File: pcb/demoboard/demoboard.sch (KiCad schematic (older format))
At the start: 32 parts, among them J1 BTN, J10 Conn_01x15, J11 Servo2, J12 TEMP, J13 MOT_A, J14 MOT_B, J15 CAP_T, J16 ANALOG, J17 7SEG1, J18 7SEG2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

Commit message: PCB 0.1
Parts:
- removed J15: CAP_T, Connector_PinSocket_2.54mm:PinSocket_1x04_P2.54mm_Vertical, symbol Connector_Generic:Conn_01x04
- removed J21: BITS, Connector_PinSocket_2.54mm:PinSocket_1x10_P2.54mm_Vertical, symbol Connector_Generic:Conn_01x10
- removed U3: PCF8574, Package_DIP:DIP-16_W7.62mm, symbol Interface_Expansion:PCF8574
- added R5: 4K7, Resistor_THT:R_Axial_DIN0207_L6.3mm_D2.5mm_P10.16mm_Horizontal, symbol Device:R
- added U1: 74HC595, Package_DIP:DIP-16_W7.62mm, symbol 74xx:74HC595
- J1: footprint Connector_PinSocket_2.54mm:PinSocket_1x03_P2.54mm_Vertical -> Connector_PinSocket_2.54mm:PinSocket_1x03_P2.54mm_Horizontal
- R2, R3: value 4K7 -> 220R; footprint Resistor_THT:R_Axial_DIN0207_L6.3mm_D2.5mm_P10.16mm_Horizontal -> Resistor_THT:R_Axial_DIN0207_L6.3mm_D2.5mm_P2.54mm_Vertical
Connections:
- net D35 is gone; now on net BTN: J10.11 (Pin_11), J8.11 (Pin_11)
- net INT is gone; now on net BTN: J4.3 (Pin_3)
- net B0: now also J18.1 (Pin_1), U1.15 (QA); no longer J17.1 (Pin_1)
- net B1: now also J18.2 (Pin_2), U1.1 (QB); no longer J17.2 (Pin_2)
- net B2: now also J17.1 (Pin_1), U1.2 (QC); no longer J17.3 (Pin_3)
- net B3: now also U1.3 (QD)
- net B4: now also J17.3 (Pin_3), U1.4 (QE); no longer J17.5 (Pin_5)
- net B5: now also J18.5 (Pin_5), U1.5 (QF); no longer J18.1 (Pin_1)
- net B6: now also J17.2 (Pin_2), U1.6 (QG); no longer J18.2 (Pin_2)
- net B7: now also J17.5 (Pin_5), U1.7 (QH); no longer J18.5 (Pin_5)
- net BTN: no longer J3.10 (Pin_10), J5.10 (Pin_10)
- net D14: now also R2.1; no longer J18.3 (Pin_3)
- net D2: now also J4.1 (Pin_1)
- net D21: no longer R3.1
- net D22: no longer R2.1
- net D25: now also R3.1; no longer J18.4 (Pin_4)
- net D32: now also J6.2 (Pin_2)
- net D33: now also U1.12 (RCLK)
- net D34: now also J4.2 (Pin_2)
- net D5: now also U2.15 (4A); no longer J6.2 (Pin_2)
- net GND: now also U1.13 (~OE), U1.8 (GND)
- net MA1Y: now also J13.2 (Pin_2); no longer J13.1 (Pin_1)
- net MA2Y: now also J13.1 (Pin_1); no longer J13.2 (Pin_2)
- net MB1Y: now also J14.2 (Pin_2); no longer J14.1 (Pin_1)
- net MB2Y: now also J14.1 (Pin_1); no longer J14.2 (Pin_2)
- net VCC: now also R5.2, U1.16 (VCC); no longer R2.2, R3.2
- net BUZZ renamed D23
- net D23: now also U1.14 (SER); no longer J4.1 (Pin_1)
- net D18 renamed CLK
- net CLK: now also U1.11 (SRCLK); no longer U2.15 (4A)
- new net: J18.3 (Pin_3), R3.2
- new net: J18.4 (Pin_4), R2.2
- new net D19: J3.10 (Pin_10), J5.10 (Pin_10)
- new net SRCLR: R5.1, U1.10 (~SRCLR)
- no-connect marks 1 -> 2

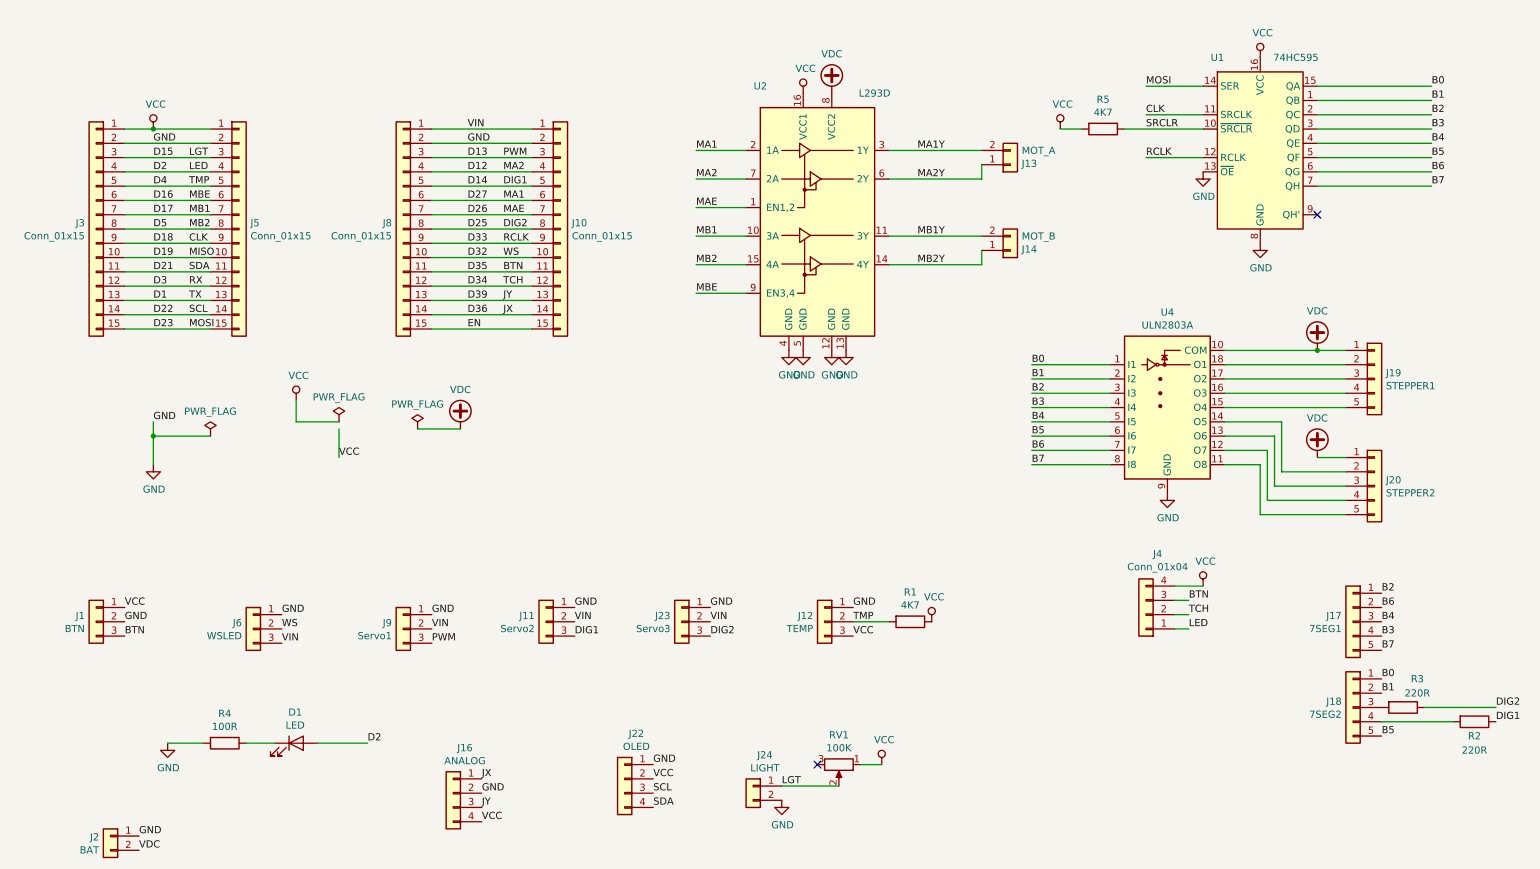
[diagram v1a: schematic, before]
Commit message: Rearrange the PCB components a bit
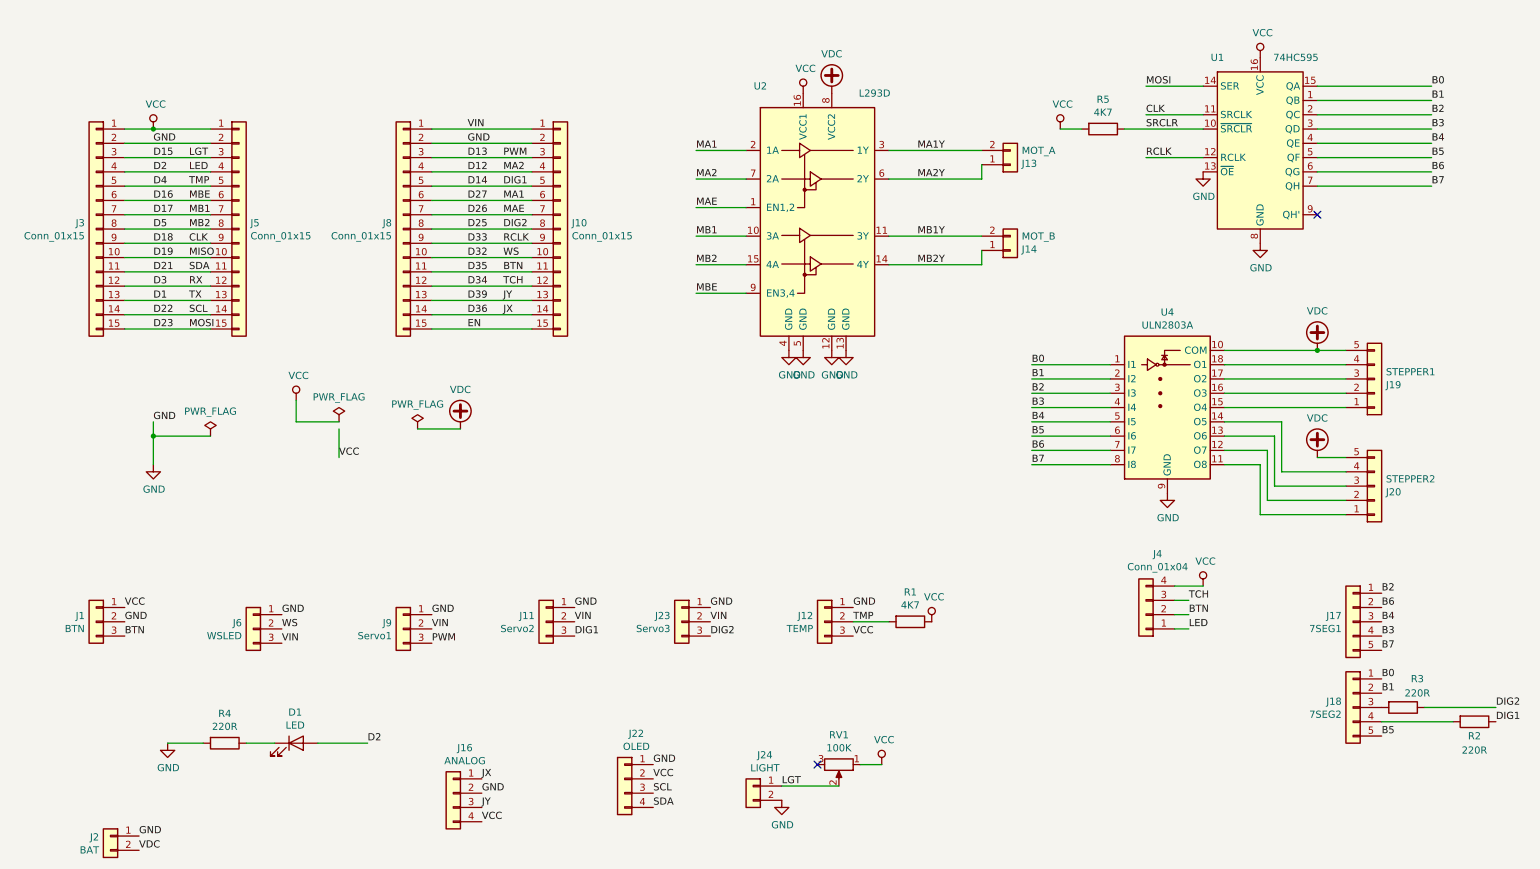
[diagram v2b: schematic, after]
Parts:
- R4: value 100R -> 220R
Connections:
- net BTN: now also J4.2 (Pin_2); no longer J4.3 (Pin_3)
- net D34: now also J4.3 (Pin_3); no longer J4.2 (Pin_2)
- net VDC: now also J19.5 (Pin_5), J20.5 (Pin_5); no longer J19.1 (Pin_1), J20.1 (Pin_1)
- net at U4.11 (O8): now also J20.1 (Pin_1); no longer J20.5 (Pin_5)
- net at U4.12 (O7): now also J20.2 (Pin_2); no longer J20.4 (Pin_4)
- net at U4.14 (O5): now also J20.4 (Pin_4); no longer J20.2 (Pin_2)
- net at U4.15 (O4): now also J19.1 (Pin_1); no longer J19.5 (Pin_5)
- net at U4.16 (O3): now also J19.2 (Pin_2); no longer J19.4 (Pin_4)
- net at U4.18 (O1): now also J19.4 (Pin_4); no longer J19.2 (Pin_2)
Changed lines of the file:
@@
 F 3 "~" H 10000 3800 50  0001 C CNN
 	1    10000 3800
-	1    0    0    -1
+	1    0    0    1
 $EndComp
 $Comp
@@
 F 3 "~" H 10000 4550 50  0001 C CNN
 	1    10000 4550
-	1    0    0    -1
+	1    0    0    1
 $EndComp
 $Comp
@@
 P 1950 6350
 F 0 "R4" V 1743 6350 50  0000 C CNN
-F 1 "100R" V 1834 6350 50  0000 C CNN
+F 1 "220R" V 1834 6350 50  0000 C CNN
 F 2 "Resistor_THT:R_Axial_DIN0207_L6.3mm_D2.5mm_P10.16mm_Horizontal" V 1880 6350 50  0001 C CNN
 F 3 "~" H 1950 6350 50  0001 C CNN
@@
 Wire Wire Line
 	8600 5350 8700 5350
-Text Label 8700 5350 0    50   ~ 0
+Text Label 8700 5450 0    50   ~ 0
 BTN
 $Comp
@@
 Text Label 8400 2050 0    50   ~ 0
 SRCLR
-Text Label 8700 5450 0    50   ~ 0
+Text Label 8700 5350 0    50   ~ 0
 TCH
 Text Label 6800 2400 0    50   ~ 0

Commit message: PCB v0.2
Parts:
- added J7: JMP, Connector_PinHeader_2.54mm:PinHeader_1x02_P2.54mm_Vertical, symbol Connector_Generic:Conn_01x02
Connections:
- net B6: now also J17.5 (Pin_5); no longer J17.2 (Pin_2)
- net B7: now also J17.2 (Pin_2); no longer J17.5 (Pin_5)
- net BTN: now also J4.3 (Pin_3); no longer J4.2 (Pin_2)
- net D13: now also J11.3 (Pin_3), R2.1; no longer J9.3 (Pin_3)
- net D14: now also J9.3 (Pin_3); no longer J11.3 (Pin_3), R2.1
- net D15: now also U2.9 (EN3,4); no longer J24.1 (Pin_1), RV1.2
- net D16: now also U2.10 (3A); no longer U2.9 (EN3,4)
- net D17: now also U2.15 (4A); no longer U2.10 (3A)
- net D25: now also J6.2 (Pin_2); no longer J23.3 (Pin_3), R3.1
- net D32: now also U1.12 (RCLK); no longer J6.2 (Pin_2)
- net D33: now also J4.2 (Pin_2); no longer U1.12 (RCLK)
- net D34: now also J24.1 (Pin_1), RV1.2; no longer J4.3 (Pin_3)
- net D5: now also J23.3 (Pin_3), R3.1; no longer U2.15 (4A)
- net GND: now also J7.1 (Pin_1)
- net VDC: now also J19.1 (Pin_1), J20.1 (Pin_1); no longer J19.5 (Pin_5), J20.5 (Pin_5)
- net at U4.11 (O8): now also J20.2 (Pin_2); no longer J20.1 (Pin_1)
- net at U4.12 (O7): now also J20.3 (Pin_3); no longer J20.2 (Pin_2)
- net at U4.13 (O6): now also J20.4 (Pin_4); no longer J20.3 (Pin_3)
- net at U4.14 (O5): now also J20.5 (Pin_5); no longer J20.4 (Pin_4)
- net at U4.15 (O4): now also J19.2 (Pin_2); no longer J19.1 (Pin_1)
- net at U4.16 (O3): now also J19.3 (Pin_3); no longer J19.2 (Pin_2)
- net at U4.17 (O2): now also J19.4 (Pin_4); no longer J19.3 (Pin_3)
- net at U4.18 (O1): now also J19.5 (Pin_5); no longer J19.4 (Pin_4)
- net at J18.3 (Pin_3): now also R2.2; no longer R3.2
- net at J18.4 (Pin_4): now also R3.2; no longer R2.2
- net RP: now reaches RV1.3
- net RP: now also J7.2 (Pin_2)
- no-connect marks 2 -> 1
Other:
- moved on the sheet: J19, J20, R2, R3
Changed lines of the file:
@@
 F 3 "~" H 6150 5500 50  0001 C CNN
 	1    6150 5500
-	-1   0    0    -1
+	-1   0    0    1
 $EndComp
 $Comp
 L Connector_Generic:Conn_01x05 J19
 U 1 1 5E2CC9BE
-P 10000 3800
-F 0 "J19" H 10080 3842 50  0000 L CNN
-F 1 "STEPPER1" H 10080 3751 50  0000 L CNN
-F 2 "Connector_PinHeader_2.54mm:PinHeader_1x05_P2.54mm_Vertical" H 10000 3800 50  0001 C CNN
-F 3 "~" H 10000 3800 50  0001 C CNN
-	1    10000 3800
+P 10000 3900
+F 0 "J19" H 10080 3942 50  0000 L CNN
+F 1 "STEPPER1" H 10080 3851 50  0000 L CNN
+F 2 "Connector_PinHeader_2.54mm:PinHeader_1x05_P2.54mm_Vertical" H 10000 3900 50  0001 C CNN
+F 3 "~" H 10000 3900 50  0001 C CNN
+	1    10000 3900
 	1    0    0    1
 $EndComp
@@
 L Connector_Generic:Conn_01x05 J20
 U 1 1 5E2CD0D9
-P 10000 4550
-F 0 "J20" H 10080 4592 50  0000 L CNN
-F 1 "STEPPER2" H 10080 4501 50  0000 L CNN
-F 2 "Connector_PinHeader_2.54mm:PinHeader_1x05_P2.54mm_Vertical" H 10000 4550 50  0001 C CNN
-F 3 "~" H 10000 4550 50  0001 C CNN
-	1    10000 4550
+P 10000 4650
+F 0 "J20" H 10080 4692 50  0000 L CNN
+F 1 "STEPPER2" H 10080 4601 50  0000 L CNN
+F 2 "Connector_PinHeader_2.54mm:PinHeader_1x05_P2.54mm_Vertical" H 10000 4650 50  0001 C CNN
+F 3 "~" H 10000 4650 50  0001 C CNN
+	1    10000 4650
 	1    0    0    1
 $EndComp
@@
 Text Label 5350 5600 0    50   ~ 0
 DIG2
-Text Label 6350 5400 0    50   ~ 0
+Text Label 6350 5600 0    50   ~ 0
 GND
 Text Label 6350 5500 0    50   ~ 0
 TMP
-Text Label 6350 5600 0    50   ~ 0
+Text Label 6350 5400 0    50   ~ 0
 VCC
 $Comp
@@
 Text Label 10050 5300 0    50   ~ 0
 B2
-Text Label 10050 5400 0    50   ~ 0
+Text Label 10050 5700 0    50   ~ 0
 B6
 Text Label 10050 5500 0    50   ~ 0
@@
 Text Label 10050 5600 0    50   ~ 0
 B3
-Text Label 10050 5700 0    50   ~ 0
+Text Label 10050 5400 0    50   ~ 0
 B7
 Text Label 10050 5900 0    50   ~ 0
@@
 Text Label 10050 6000 0    50   ~ 0
 B1
+Text Label 10850 6200 0    50   ~ 0
+DIG2
 Text Label 10850 6100 0    50   ~ 0
-DIG2
-Text Label 10850 6200 0    50   ~ 0
 DIG1
 Text Label 10050 6300 0    50   ~ 0
@@
 Wire Wire Line
 	3600 4150 3300 4150
-NoConn ~ 6100 6500
 $Comp
 L power:PWR_FLAG #FLG0103
@@
 Wire Wire Line
 	2450 4100 2750 4100
-Wire Wire Line
-	9800 4350 9600 4350
-Wire Wire Line
-	9800 3600 9600 3600
 Text Label 1700 3250 0    50   ~ 0
 TX
@@
 Text Label 3900 2350 0    50   ~ 0
 MA2
+Text Label 3900 2450 0    50   ~ 0
+PWM
 Text Label 3900 2250 0    50   ~ 0
-PWM
-Text Label 3900 2450 0    50   ~ 0
 DIG1
+Text Label 1700 2250 0    50   ~ 0
+MBE
 Text Label 1700 2550 0    50   ~ 0
-MBE
-Text Label 1700 2650 0    50   ~ 0
 MB1
 Text Label 1700 2850 0    50   ~ 0
@@
 Text Label 3900 2650 0    50   ~ 0
 MAE
-Text Label 3900 2750 0    50   ~ 0
+Text Label 1700 2750 0    50   ~ 0
 DIG2
 Text Label 1700 3450 0    50   ~ 0
@@
 Text Label 3900 2550 0    50   ~ 0
 MA1
+Text Label 3900 2750 0    50   ~ 0
+WS
 Text Label 3900 2950 0    50   ~ 0
-WS
-Text Label 3900 2850 0    50   ~ 0
 RCLK
 Text Label 3900 3050 0    50   ~ 0
 BTN
-Text Label 3900 3150 0    50   ~ 0
+Text Label 3900 2850 0    50   ~ 0
 TCH
 Text Label 3900 3350 0    50   ~ 0
@@
 Text Label 3900 3250 0    50   ~ 0
 JY
-Text Label 1700 2750 0    50   ~ 0
+Text Label 1700 2650 0    50   ~ 0
 MB2
-Text Label 1700 2250 0    50   ~ 0
+Text Label 3900 3150 0    50   ~ 0
 LGT
 Text Label 6800 2800 0    50   ~ 0
@@
 L power:VDC #PWR0106
 U 1 1 5E444DC5
-P 9600 3600
-F 0 "#PWR0106" H 9600 3500 50  0001 C CNN
-F 1 "VDC" H 9600 3875 50  0000 C CNN
-F 2 "" H 9600 3600 50  0001 C CNN
-F 3 "" H 9600 3600 50  0001 C CNN
-	1    9600 3600
-	1    0    0    -1
-$EndComp
-$Comp
-L power:VDC #PWR0114
-U 1 1 5E445402
-P 9600 4350
-F 0 "#PWR0114" H 9600 4250 50  0001 C CNN
-F 1 "VDC" H 9600 4625 50  0000 C CNN
-F 2 "" H 9600 4350 50  0001 C CNN
-F 3 "" H 9600 4350 50  0001 C CNN
-	1    9600 4350
-	1    0    0    -1
-$EndComp
-Connection ~ 9600 3600
+P 10700 4150
+F 0 "#PWR0106" H 10700 4050 50  0001 C CNN
+F 1 "VDC" H 10700 4425 50  0000 C CNN
+F 2 "" H 10700 4150 50  0001 C CNN
+F 3 "" H 10700 4150 50  0001 C CNN
+	1    10700 4150
+	1    0    0    -1
+$EndComp
 Wire Wire Line
 	8950 3600 9600 3600
@@
 Wire Wire Line
 	8600 5350 8700 5350
-Text Label 8700 5450 0    50   ~ 0
+Text Label 8700 5350 0    50   ~ 0
 BTN
 $Comp
@@
 Text Label 8400 2050 0    50   ~ 0
 SRCLR
-Text Label 8700 5350 0    50   ~ 0
+Text Label 8700 5450 0    50   ~ 0
 TCH
 Text Label 6800 2400 0    50   ~ 0
@@
 L Device:R R3
 U 1 1 5E623362
-P 10200 6100
-F 0 "R3" V 10000 6200 50  0000 C CNN
-F 1 "220R" V 10100 6200 50  0000 C CNN
-F 2 "Resistor_THT:R_Axial_DIN0207_L6.3mm_D2.5mm_P2.54mm_Vertical" V 10130 6100 50  0001 C CNN
-F 3 "~" H 10200 6100 50  0001 C CNN
-	1    10200 6100
-	0    1    1    0
-$EndComp
-$Comp
-L Device:R R2
-U 1 1 5E623A2A
 P 10700 6200
-F 0 "R2" V 10800 6200 50  0000 C CNN
-F 1 "220R" V 10900 6200 50  0000 C CNN
+F 0 "R3" V 10800 6300 50  0000 C CNN
+F 1 "220R" V 10900 6300 50  0000 C CNN
 F 2 "Resistor_THT:R_Axial_DIN0207_L6.3mm_D2.5mm_P2.54mm_Vertical" V 10630 6200 50  0001 C CNN
 F 3 "~" H 10700 6200 50  0001 C CNN
@@
 	0    1    1    0
 $EndComp
+$Comp
+L Device:R R2
+U 1 1 5E623A2A
+P 10350 6100
+F 0 "R2" V 10150 6100 50  0000 C CNN
+F 1 "220R" V 10250 6100 50  0000 C CNN
+F 2 "Resistor_THT:R_Axial_DIN0207_L6.3mm_D2.5mm_P2.54mm_Vertical" V 10280 6100 50  0001 C CNN
+F 3 "~" H 10350 6100 50  0001 C CNN
+	1    10350 6100
+	0    1    1    0
+$EndComp
 Wire Wire Line
 	10050 6200 10550 6200
-Wire Wire Line
-	10350 6100 10850 6100
 Wire Wire Line
 	8250 2050 8800 2050
@@
 Wire Wire Line
 	7950 2050 7800 2050
+$Comp
+L Connector_Generic:Conn_01x02 J7
+U 1 1 5E5BD38E
+P 5650 6100
+F 0 "J7" H 5568 6317 50  0000 C CNN
+F 1 "JMP" H 5568 6226 50  0000 C CNN
+F 2 "Connector_PinHeader_2.54mm:PinHeader_1x02_P2.54mm_Vertical" H 5650 6100 50  0001 C CNN
+F 3 "~" H 5650 6100 50  0001 C CNN
+	1    5650 6100
+	-1   0    0    -1
+$EndComp
+Wire Wire Line
+	6100 6500 6100 6200
+Wire Wire Line
+	6100 6200 5850 6200
+$Comp
+L power:GND #PWR08
+U 1 1 5E5C6F26
+P 6750 6100
+F 0 "#PWR08" H 6750 5850 50  0001 C CNN
+F 1 "GND" H 6755 5927 50  0000 C CNN
+F 2 "" H 6750 6100 50  0001 C CNN
+F 3 "" H 6750 6100 50  0001 C CNN
+	1    6750 6100
+	1    0    0    -1
+$EndComp
+$Comp
+L power:VDC #PWR0114
+U 1 1 5E5CF480
+P 9600 3600
+F 0 "#PWR0114" H 9600 3500 50  0001 C CNN
+F 1 "VDC" H 9600 3875 50  0000 C CNN
+F 2 "" H 9600 3600 50  0001 C CNN
+F 3 "" H 9600 3600 50  0001 C CNN
+	1    9600 3600
+	1    0    0    -1
+$EndComp
+Wire Wire Line
+	9800 4100 9800 4300
+Wire Wire Line
+	9800 4300 10700 4300
+Wire Wire Line
+	10700 4300 10700 4150
+Wire Wire Line
+	10700 4300 10700 5000
+Wire Wire Line
+	10700 5000 9800 5000
+Wire Wire Line
+	9800 5000 9800 4850
+Connection ~ 10700 4300
+Wire Wire Line
+	5850 6100 6750 6100
+Text Label 5950 6200 0    50   ~ 0
+RP
+Wire Wire Line
+	10500 6100 10850 6100
+Wire Wire Line
+	10050 6100 10200 6100
 $EndSCHEMATC
